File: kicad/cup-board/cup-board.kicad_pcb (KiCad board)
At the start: 4 copper layers, 72 x 72 mm, 101 parts, among them J10 MK2 flex (IM73A135), J11 MK3 flex (IM72D128 PDM), J2 EARCUP_SPKR, J7 CUP_IN (A2B + panel audio, ma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, J8 CUP_OUT (A2B to next cup), J9 MK1 flex (IM73A135 FF/FB), Q1 AO3401A, Q2 MMBT3904, U1 ADAU1861, U2 LSM6DSV16BX, U3 MAXM86161, U4 AQW612S, U5 AQW612S, U6 AD2428WBCPZ (sub-node), U7 TPS62161DSG (1V8), U8 ADP7118AUJZ-3.3-R7 (3V3_MIC), U9 ADP7118AUJZ-3.3-R7 (VLED)

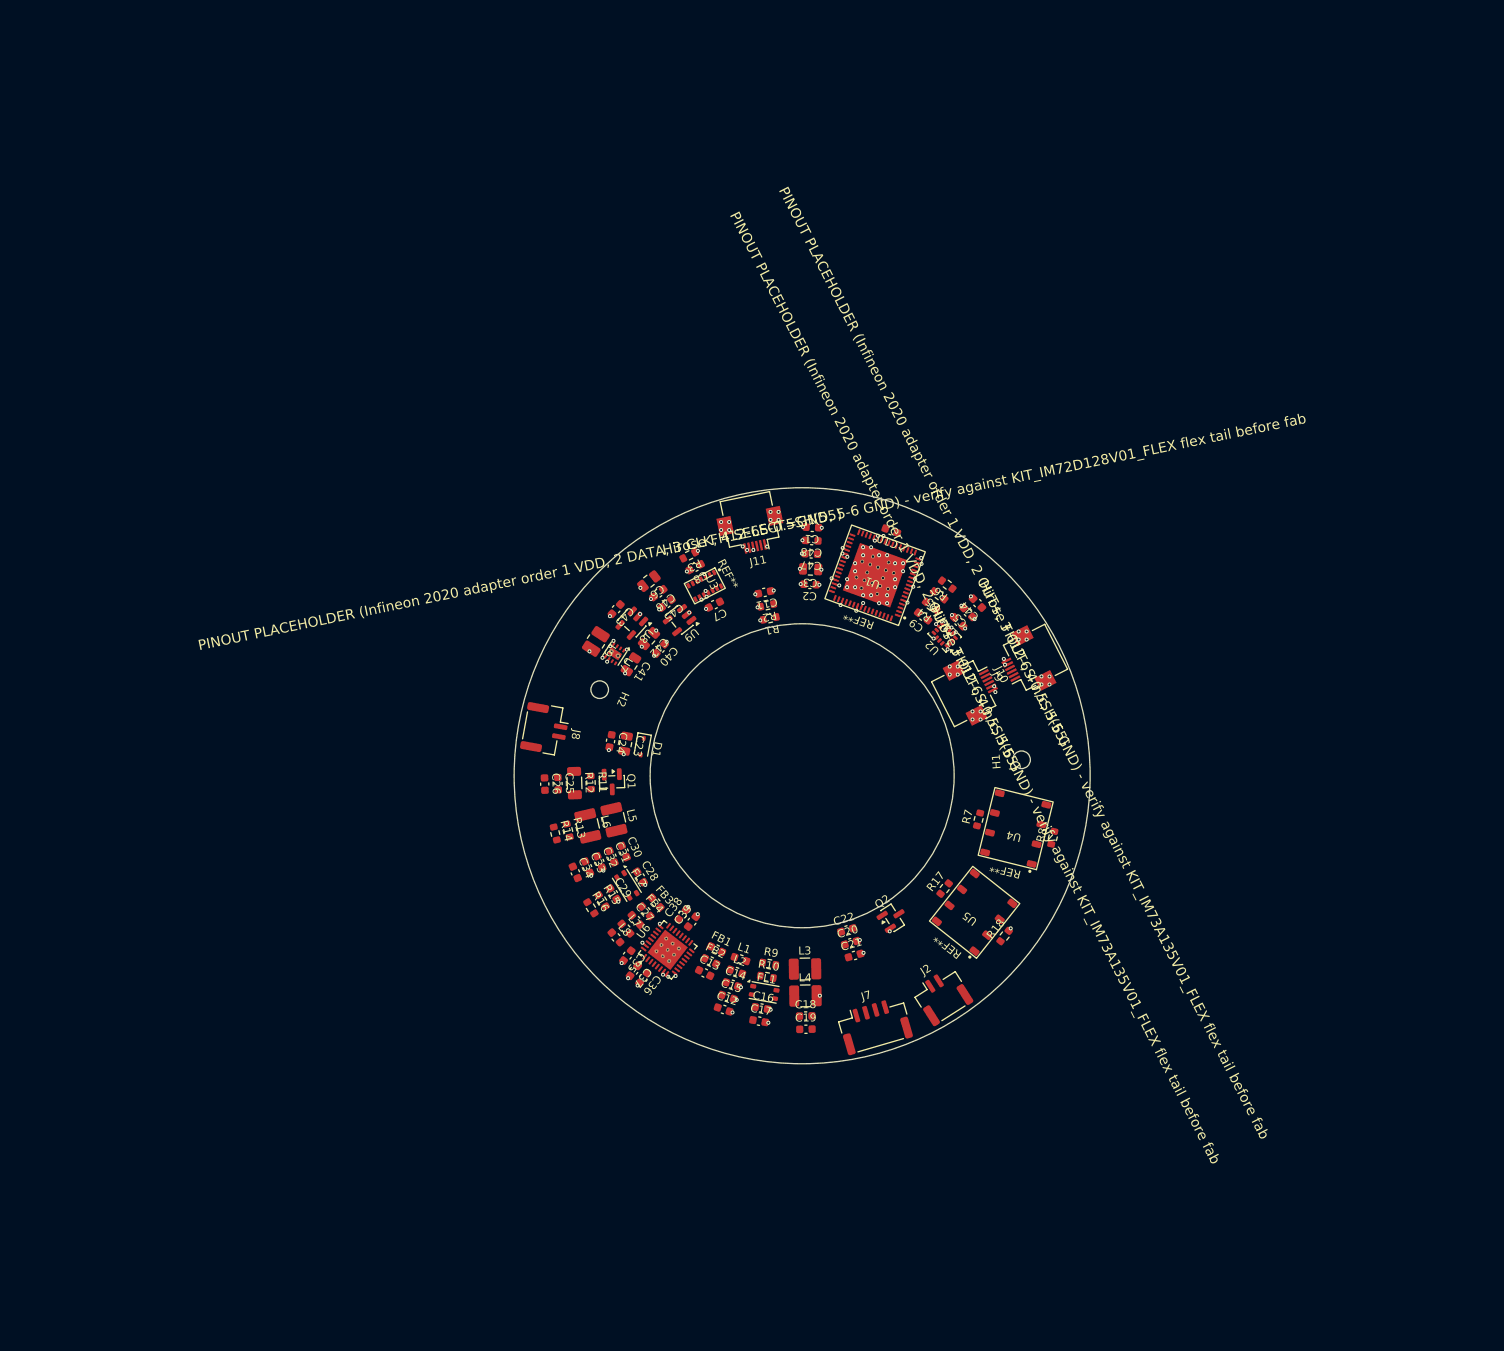
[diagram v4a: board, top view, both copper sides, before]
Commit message: [LIMA] cup PCB 72/38: Freerouting pass (WIP) - 23 unconnected, 0 clearance errors; ZIF fields hidden on silk
Co-Authored-By: Claude Opus 5.5 <noreply@anthropic.com>
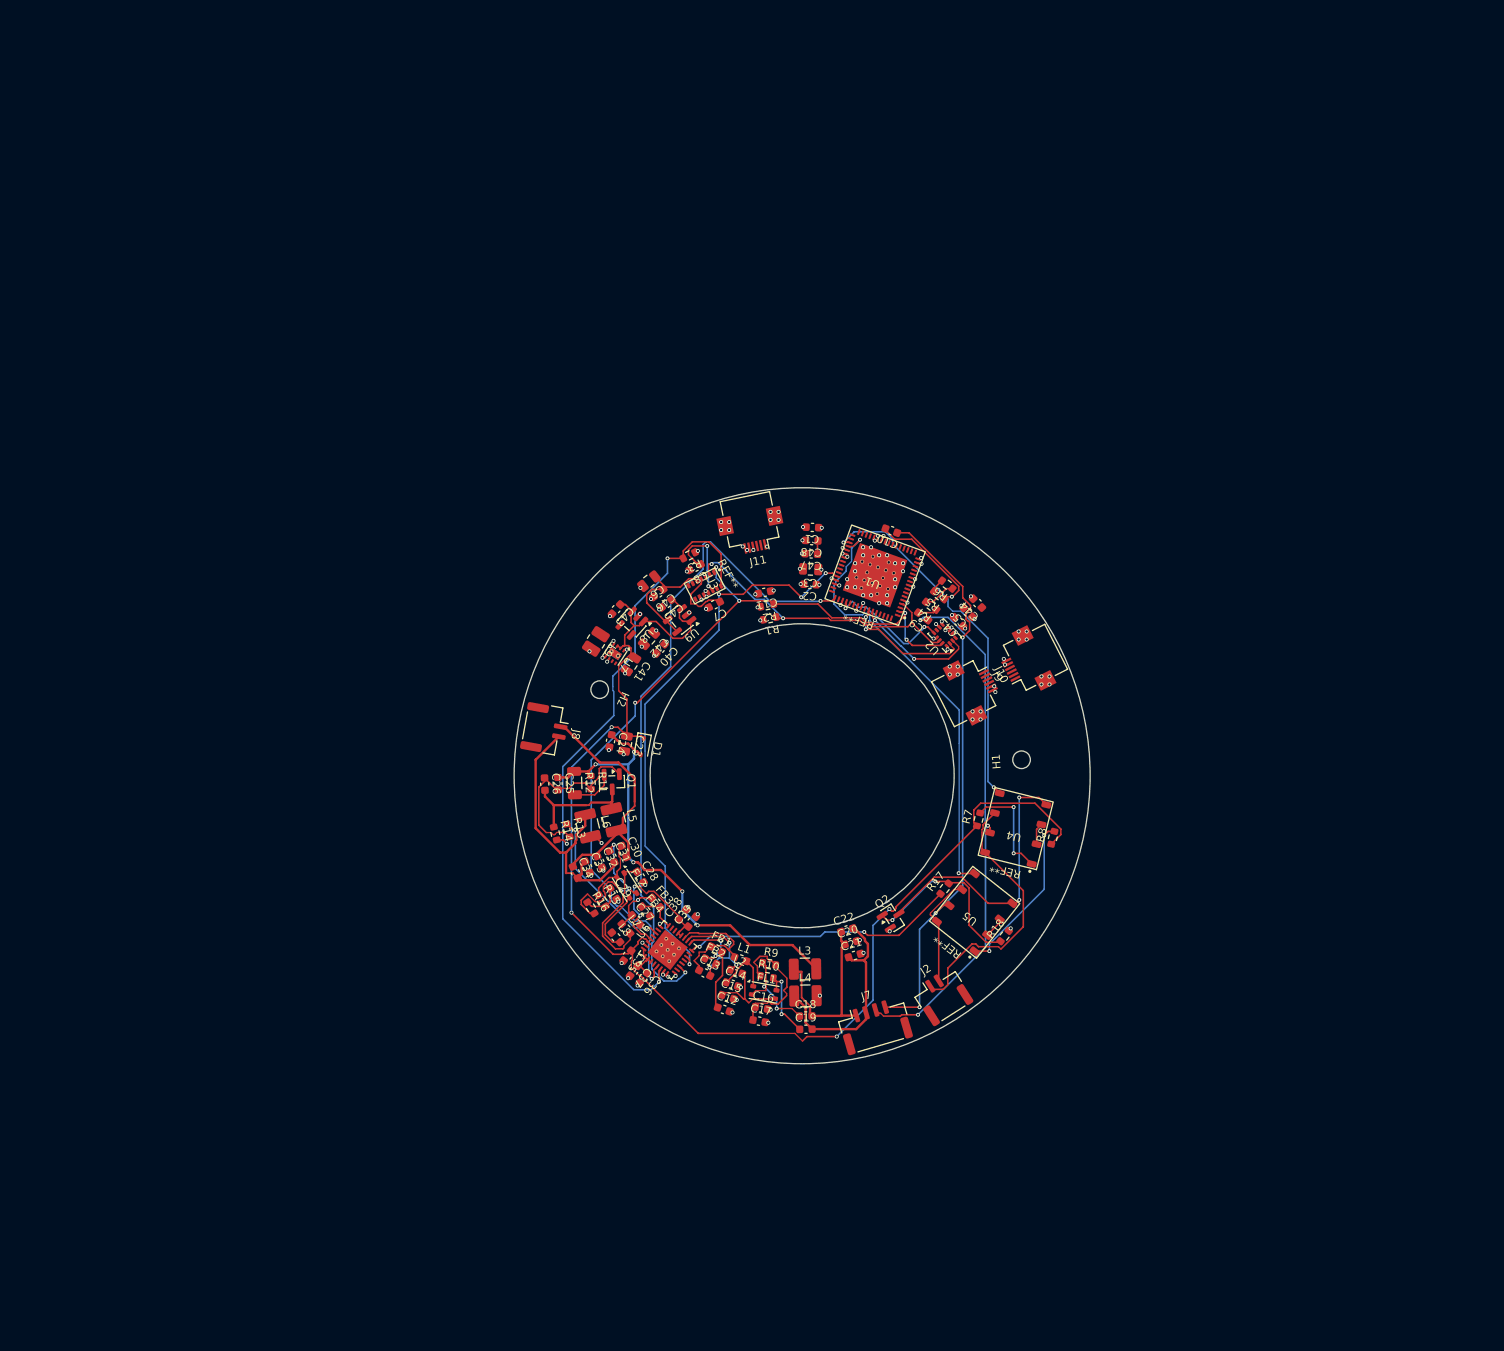
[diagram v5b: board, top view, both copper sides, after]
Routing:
- net /VIN_CUP: track 0.00 -> 162.7 mm, vias 0 -> 4
- net /SDA: track 0.00 -> 99.2 mm, vias 0 -> 6
- net /I2S0_FSYNC: track 0.00 -> 83.2 mm, vias 0 -> 2
- net /PPG_INT: track 0.00 -> 81.1 mm, vias 0 -> 2
- net /XF_SEC_B: track 0.00 -> 73.5 mm, vias 0 -> 3
- net /I2S0_SDATAO: track 0.00 -> 70.7 mm, vias 0 -> 4
- net /XF_SEC_A: track 0.00 -> 66.6 mm, vias 0 -> 3
- net /V_NODE: track 0.00 -> 59.2 mm, vias 0 -> 5
- net /HPOUTP: track 0.00 -> 55.4 mm, vias 0 -> 2
- net /HPOUTN: track 0.00 -> 45.8 mm, vias 0 -> 2
- net /SCL: track 0.00 -> 38.9 mm, vias 0 -> 2
- net /B_LINE_N: track 0.00 -> 36.0 mm
- net /K2_SW: track 0.00 -> 35.1 mm, vias 0 -> 2
- net /K2_CTL: track 0.00 -> 34.4 mm, vias 0 -> 2
- net /SPKR_1: track 0.00 -> 33.8 mm
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
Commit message: [LIMA] cup PCB 72/38: B trio routed first + rip-up finish - 7 unconnected, 0 errors (WIP)
Co-Authored-By: Claude Opus 5.5 <noreply@anthropic.com>
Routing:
- net /I2S0_BCLK: track 0.00 -> 66.4 mm, vias 0 -> 4
- net /3V3_MIC: track 0.00 -> 66.1 mm, vias 0 -> 2
- net /I2S0_SDATAI: track 0.00 -> 63.5 mm, vias 0 -> 2
- net /SCL: track 38.9 -> 91.0 mm, vias 2 -> 6
- net /VIN_CUP: track 162.7 -> 116.9 mm, vias 4 -> 8
- net /GND: track 30.8 -> 61.7 mm, vias 115 -> 113
- net /MK1_OUTP: track 0.00 -> 26.1 mm, vias 0 -> 3
- net /MK1_OUTN: track 0.00 -> 22.6 mm, vias 0 -> 2
- net /I2S0_FSYNC: track 83.2 -> 66.1 mm, vias 2 -> 5
- net Net-(C10-Pad2): track 15.0 -> 0.00 mm, vias 1 -> 0
- net /A2B_VOUT2: track 19.6 -> 5.75 mm
- net /B_VSSN: track 1.73 -> 14.9 mm, vias 1 -> 4
- net /U1_DVDD: track 1.69 -> 11.1 mm, vias 0 -> 2
- net /ADC2_P: track 4.00 -> 13.2 mm, vias 0 -> 2
- net /ADC2_N: track 1.74 -> 9.30 mm, vias 0 -> 2
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
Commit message: [LIMA] cup PCB: second finishing stage - 6 unconnected (5 nets + 1V8 plane split on In2), 0 errors (WIP)
ripnets.py --local (rip only near pads), fanout.py FANOUT_PADS (repair one pad).

Co-Authored-By: Claude Opus 5.5 <noreply@anthropic.com>
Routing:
- net /K2_CTL: track 33.8 -> 10.9 mm, vias 4 -> 3
- net /ADC2_N: track 9.30 -> 31.4 mm, vias 2 -> 5
- net /MK2_OUTP: track 0.00 -> 22.1 mm, vias 0 -> 2
- net /DMIC_DATA: track 0.00 -> 20.7 mm, vias 0 -> 2
- net /SCL: track 91.0 -> 108.6 mm, vias 6 -> 12
- net /XF_SEC_A: track 66.6 -> 56.7 mm
- net /HPOUTP: track 55.4 -> 60.5 mm
- net /XF_SEC_B: track 73.5 -> 69.6 mm, vias 3 -> 6
- net /MK1_OUTP: track 26.1 -> 24.5 mm, vias 3 -> 2
- net /3V3_MIC: track 66.1 -> 64.5 mm, vias 2 -> 4
- net /ADC2_P: track 13.2 -> 13.6 mm, vias 2 -> 5
- net /SDA: track 102.8 -> 103.1 mm, vias 7 -> 6
- net /1V8: track 15.7 -> 16.0 mm, vias 26 -> 25

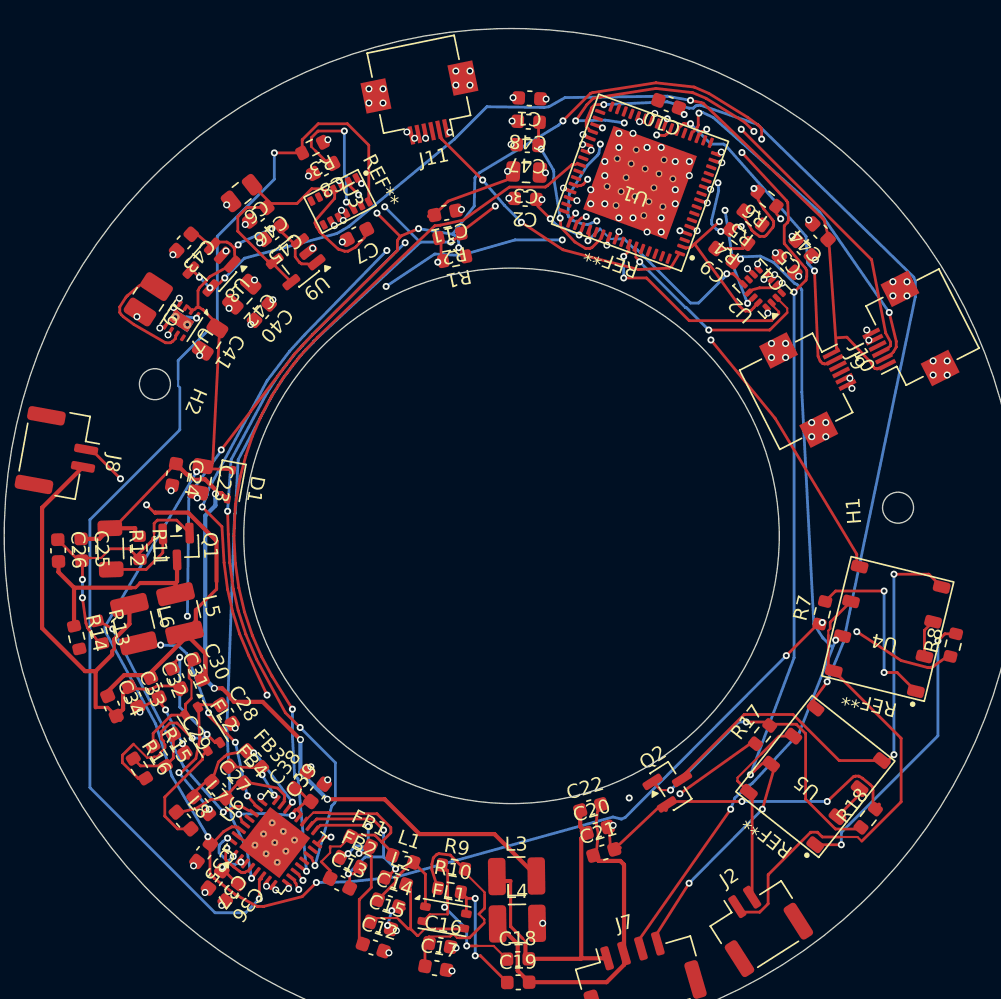
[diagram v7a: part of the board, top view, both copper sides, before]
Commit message: [LIMA] cup PCB: U1 quadrant re-routed mic-first - 2 unconnected, 0 errors, 1V8 plane whole (WIP)
Co-Authored-By: Claude Opus 5.5 <noreply@anthropic.com>
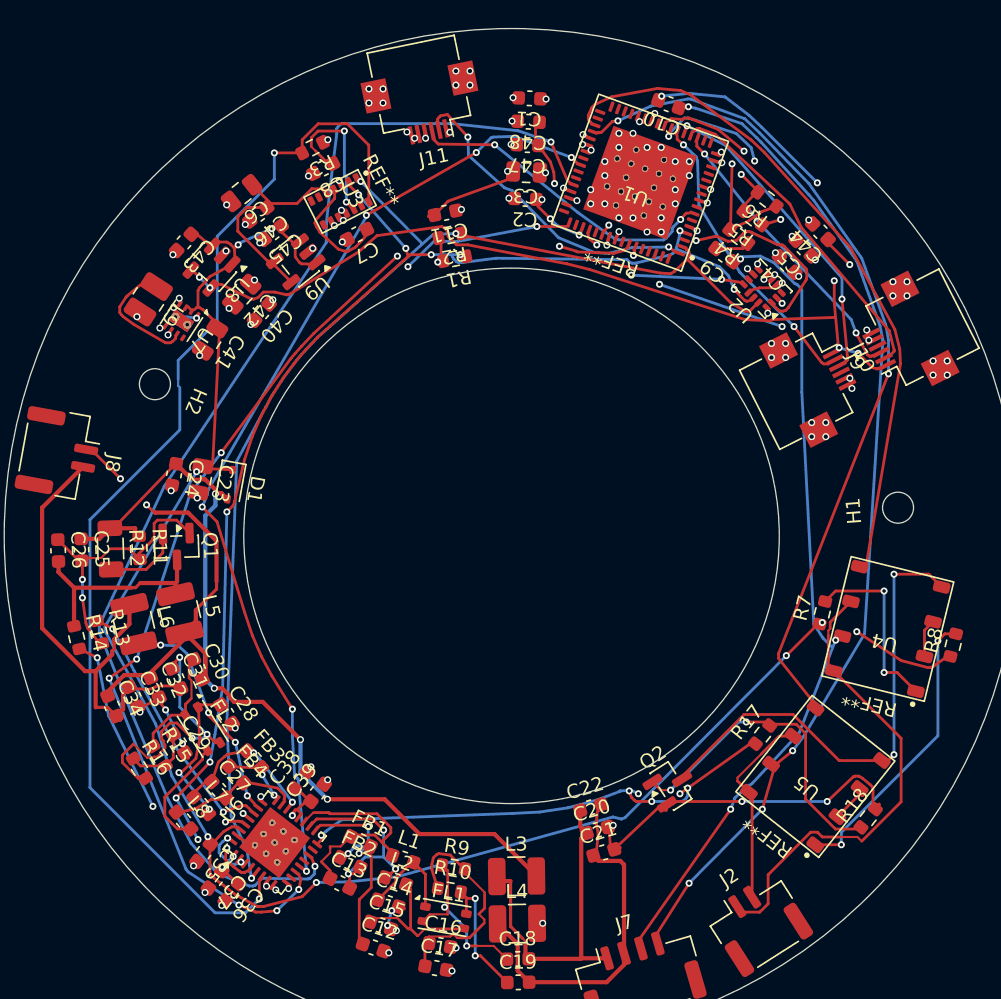
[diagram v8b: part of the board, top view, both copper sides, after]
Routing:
- net /I2S0_BCLK: track 66.4 -> 0.00 mm, vias 4 -> 0
- net /K2_CTL: track 10.9 -> 35.6 mm, vias 3 -> 6
- net /MK2_OUTN: track 0.00 -> 21.8 mm, vias 0 -> 2
- net /DMIC_CLK: track 0.00 -> 21.5 mm, vias 0 -> 2
- net /SCL: track 108.6 -> 87.4 mm, vias 12 -> 11
- net /SDA: track 103.1 -> 83.0 mm, vias 6 -> 3
- net /I2S0_SDATAO: track 66.5 -> 86.6 mm, vias 5 -> 2
- net /ADC2_N: track 31.4 -> 11.7 mm, vias 5 -> 3
- net /B_SENSE: track 0.00 -> 19.6 mm, vias 0 -> 3
- net Net-(C10-Pad2): track 0.00 -> 18.0 mm, vias 0 -> 3
- net /TDM_DATA: track 16.0 -> 28.2 mm
- net /I2S0_FSYNC: track 66.1 -> 75.4 mm, vias 5 -> 9
- net /HPOUTN: track 40.3 -> 47.7 mm, vias 4 -> 0
- net /I2S0_SDATAI: track 63.5 -> 68.4 mm, vias 2 -> 6
- net /3V3_MIC: track 64.5 -> 60.1 mm, vias 4 -> 6
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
